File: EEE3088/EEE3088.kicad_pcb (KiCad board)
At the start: 2 copper layers, 6 parts, among them U1 LTR-303ALS-01, U2 LTR-303ALS-01

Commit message: Lecture_PCB_Updates
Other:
- board outline added: 177.8 x 83.8 mm
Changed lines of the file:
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@@
   )
   (setup
+    (stackup
+      (layer "F.SilkS" (type "Top Silk Screen"))
+      (layer "F.Paste" (type "Top Solder Paste"))
+      (layer "F.Mask" (type "Top Solder Mask") (thickness 0.01))
+      (layer "F.Cu" (type "copper") (thickness 0.035))
+      (layer "dielectric 1" (type "core") (thickness 1.51) (material "FR4") (epsilon_r 4.5) (loss_tangent 0.02))
+      (layer "B.Cu" (type "copper") (thickness 0.035))
+      (layer "B.Mask" (type "Bottom Solder Mask") (thickness 0.01))
+      (layer "B.Paste" (type "Bottom Solder Paste"))
+      (layer "B.SilkS" (type "Bottom Silk Screen"))
+      (copper_finish "None")
+      (dielectric_constraints no)
+    )
     (pad_to_mask_clearance 0)
     (pcbplotparams
@@
     )
   )
+  (gr_rect (start 40.64 43.18) (end 218.44 127)
+    (stroke (width 0.1) (type default)) (fill none) (layer "Edge.Cuts"))
 )

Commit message: Started Microcontroller PCB
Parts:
- added 0 Ohm: RESC1005X40N, 0 Ohm Resistor:RESC1005X40N, F.Cu at (148.4, 86.1)
- added 0 Ohm: RESC1005X40N, 0 Ohm Resistor:RESC1005X40N, F.Cu at (128.1, 98.8)
- added 1.8k Ohm: RESC2013X65N, 1.8k Ohm Resistor:RESC2013X65N, F.Cu at (125.6, 75.9)
- added 1.8k Ohm: RESC2013X65N, 1.8k Ohm Resistor:RESC2013X65N, F.Cu at (125.6, 81.0)
- added CH340G Bridge: SOIC127P600X180-16N, CH340G Bridge:SOIC127P600X180-16N, F.Cu at (140.8, 91.2)
- added EEPROM Chip: SOIC127P600X175-8N, AT24C256C-SSHL-T EEPROM Chip:SOIC127P600X175-8N, F.Cu at (125.4, 89.3)
- added MICROXNJ USB Interface: SHOUHAN_MICROXNJ, MICROXNJ USB Interface:SHOUHAN_MICROXNJ, F.Cu at (140.7, 74.1)
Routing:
- net (no net): track 0.00 -> 86.4 mm
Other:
- board text added: "5V from USB"
- board text added: "D-"
- board text added: "GND"
- board text added: "Microcontroller Interfacing Module"

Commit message: Finished uC PCB connections
Your mom helped
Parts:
- moved 1.8k Ohm 47.9 mm to (170.2, 63.5), turned to -90 degrees
- moved EEPROM Chip 42.7 mm to (154.9, 58.4)
- moved 0 Ohm 42.0 mm to (154.4, 66.0)
- moved 1.8k Ohm 39.9 mm to (162.6, 61.0), turned to -90 degrees
- moved CH340G Bridge 25.2 mm to (139.7, 66.0), turned to 90 degrees
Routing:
- net (no net): track 86.4 -> 309.4 mm
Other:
- board text added: "Needs to go to 3.3V"
- board text added: "Needs to go to GND"
- board text added: "RXD"
- board text added: "SCL"
- board text added: "SDA"
- board text added: "TIMIN"
- board text added: "TIMOUT"
- board text added: "TXD"
- board text removed: "Microcontroller Interfacing Module"

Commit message: pcb_Sense_Initial
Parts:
- added C3: 1uF, Capacitor_SMD:C_0805_2012Metric, F.Cu at (54.9, 95.2)
- added C4: 1uF, Capacitor_SMD:C_0805_2012Metric, F.Cu at (144.8, 95.2)
- added C9: 1uF, Capacitor_SMD:C_0805_2012Metric, F.Cu at (244.9, 109.6)
- added R10: 0, Resistor_SMD:R_0402_1005Metric, F.Cu at (226.0, 121.1)
- added R11: 0, Resistor_SMD:R_0402_1005Metric, F.Cu at (135.1, 137.2)
- added R12: 0, Resistor_SMD:R_0402_1005Metric, F.Cu at (66.5, 137.2)
- added R13: 0, Resistor_SMD:R_0402_1005Metric, F.Cu at (66.5, 55.9)
- added R18: 0, Resistor_SMD:R_0402_1005Metric, F.Cu at (60.5, 100.3)
- added R19: 0, Resistor_SMD:R_0402_1005Metric, F.Cu at (60.5, 99.1)
- added R20: 0, Resistor_SMD:R_0402_1005Metric, F.Cu at (140.5, 100.3)
- added R21: 0, Resistor_SMD:R_0402_1005Metric, F.Cu at (140.5, 99.1)
- added R22: 10K, Resistor_SMD:R_0805_2012Metric, F.Cu at (139.7, 106.7)
- added R23: 10K, Resistor_SMD:R_0805_2012Metric, F.Cu at (55.9, 107.6)
- added R24: 10K, Resistor_SMD:R_0805_2012Metric, F.Cu at (144.8, 106.7)
- added R25: 10K, Resistor_SMD:R_0805_2012Metric, F.Cu at (61.0, 107.6)
- added R26: 10K, Resistor_SMD:R_0805_2012Metric, F.Cu at (142.2, 106.7)
- added R27: 10K, Resistor_SMD:R_0805_2012Metric, F.Cu at (58.4, 107.6)
- added R30: 0, Resistor_SMD:R_0402_1005Metric, F.Cu at (259.2, 93.9)
- added R31: 0, Resistor_SMD:R_0402_1005Metric, F.Cu at (259.2, 95.9)
- added R4: 0, Resistor_SMD:R_0402_1005Metric, F.Cu at (226.0, 113.1)
- added R6: 0, Resistor_SMD:R_0402_1005Metric, F.Cu at (226.0, 115.1)
- added R8: 0, Resistor_SMD:R_0402_1005Metric, F.Cu at (226.0, 117.1)
- added R9: 0, Resistor_SMD:R_0402_1005Metric, F.Cu at (226.0, 119.1)
- added TP1: TestPoint, TestPoint:TestPoint_Pad_2.0x2.0mm, F.Cu at (245.2, 115.6)
- added TP10: TestPoint, TestPoint:TestPoint_Pad_2.0x2.0mm, F.Cu at (134.6, 97.8)
- added TP11: TestPoint, TestPoint:TestPoint_Pad_2.0x2.0mm, F.Cu at (64.8, 105.4)
- added TP13: TestPoint, TestPoint:TestPoint_Pad_2.0x2.0mm, F.Cu at (245.2, 95.4)
- added TP14: TestPoint, TestPoint:TestPoint_Pad_2.0x2.0mm, F.Cu at (245.2, 100.5)
- added TP15: TestPoint, TestPoint:TestPoint_Pad_2.0x2.0mm, F.Cu at (245.2, 105.5)
- added TP16: TestPoint, TestPoint:TestPoint_Pad_2.0x2.0mm, F.Cu at (250.2, 95.4)
- added TP17: TestPoint, TestPoint:TestPoint_Pad_2.0x2.0mm, F.Cu at (250.2, 100.5)
- added TP18: TestPoint, TestPoint:TestPoint_Pad_2.0x2.0mm, F.Cu at (250.2, 105.5)
- added TP19: TestPoint, TestPoint:TestPoint_Pad_2.0x2.0mm, F.Cu at (255.3, 95.4)
- added TP2: TestPoint, TestPoint:TestPoint_Pad_2.0x2.0mm, F.Cu at (245.2, 120.7)
- added TP20: TestPoint, TestPoint:TestPoint_Pad_2.0x2.0mm, F.Cu at (255.3, 100.5)
- added TP21: TestPoint, TestPoint:TestPoint_Pad_2.0x2.0mm, F.Cu at (255.3, 105.5)
- added TP22: TestPoint, TestPoint:TestPoint_Pad_2.0x2.0mm, F.Cu at (255.3, 120.7)
- added TP3: TestPoint, TestPoint:TestPoint_Pad_2.0x2.0mm, F.Cu at (250.2, 115.6)
- added TP4: TestPoint, TestPoint:TestPoint_Pad_2.0x2.0mm, F.Cu at (250.2, 120.7)
- added TP5: TestPoint, TestPoint:TestPoint_Pad_2.0x2.0mm, F.Cu at (255.3, 115.6)
- added TP6: TestPoint, TestPoint:TestPoint_Pad_2.0x2.0mm, F.Cu at (135.9, 66.0)
- added TP7: TestPoint, TestPoint:TestPoint_Pad_2.0x2.0mm, F.Cu at (64.8, 66.0)
- added TP8: TestPoint, TestPoint:TestPoint_Pad_2.0x2.0mm, F.Cu at (64.8, 97.8)
- added TP9: TestPoint, TestPoint:TestPoint_Pad_2.0x2.0mm, F.Cu at (134.6, 92.7)
- moved R17 226.2 mm to (142.2, 137.2), turned to -90 degrees
- moved U1 217.1 mm to (145.4, 100.7), turned to -90 degrees
- moved R16 206.8 mm to (142.2, 54.6), turned to -90 degrees
- moved R15 167.0 mm to (58.4, 137.2), turned to -90 degrees
- moved U2 138.1 mm to (55.2, 100.7), turned to -90 degrees
- moved R14 128.8 mm to (58.4, 54.6), turned to -90 degrees
- moved 0 Ohm 77.1 mm to (228.1, 43.2)
- moved CH340G Bridge 77.1 mm to (213.4, 43.2)
- moved 0 Ohm 77.1 mm to (222.1, 63.2)
- moved 1.8k Ohm 77.1 mm to (236.2, 38.1)
- moved 1.8k Ohm 77.1 mm to (243.8, 40.6)
- moved EEPROM Chip 77.1 mm to (228.6, 35.6)
- moved MICROXNJ USB Interface 77.1 mm to (214.4, 51.2)
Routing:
- net (no net): vias 0 -> 2
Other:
- board size 177.8 x 83.8 mm -> 100 x 100 mm

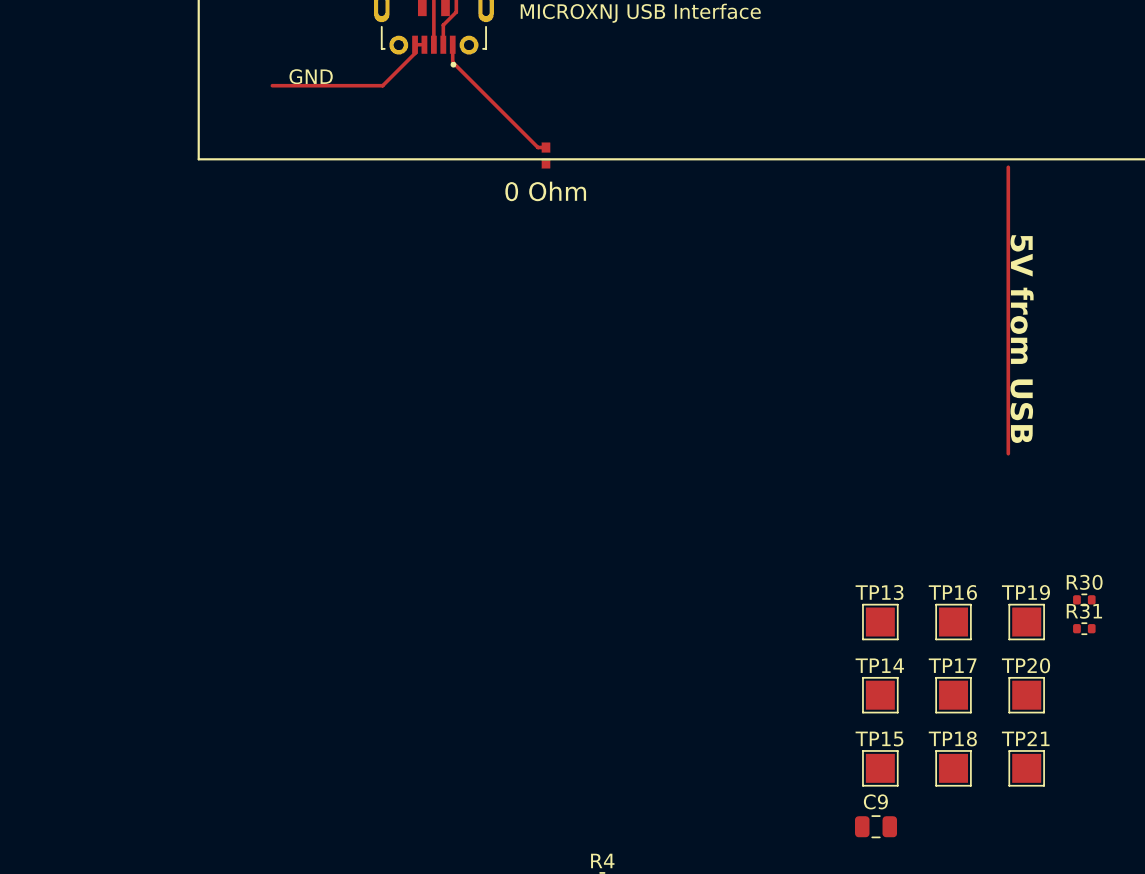
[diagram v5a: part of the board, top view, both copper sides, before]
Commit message: uC parts added onto PCB properly
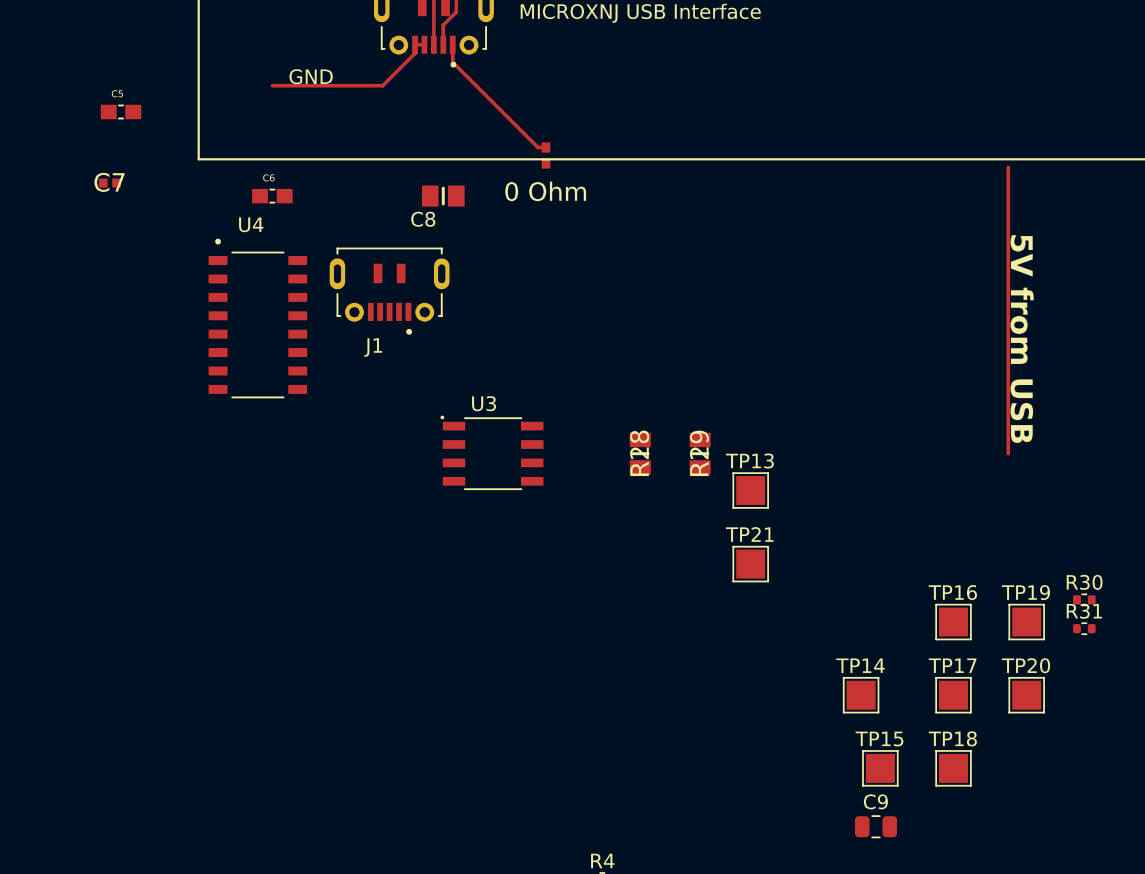
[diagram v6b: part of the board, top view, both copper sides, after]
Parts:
- added C5: 100nF, 100n CC0603KRX7R9BB104:CAPC1608X90, F.Cu at (192.8, 60.2)
- added C6: 100nF, 100n CC0603KRX7R9BB104:CAPC1608X90, F.Cu at (203.2, 66.0)
- added C7: 4.7uF, 4.7n Cap LIB_0402B472K500NT:CAPC1005X55N, F.Cu at (192.0, 65.1)
- added C8: 10nF, 10n Cap CL21B103KBANNNC:CAPC2012X140N, F.Cu at (215.0, 66.0)
- added J1: MICROXNJ, MICROXNJ:SHOUHAN_MICROXNJ, F.Cu at (211.3, 69.7)
- added R28: 1.8k, 1.8k Ohm Resistor:RESC2013X65N, F.Cu at (228.6, 83.8)
- added R29: 1.8k, 1.8k Ohm Resistor:RESC2013X65N, F.Cu at (232.7, 83.8)
- added U3: AT24C256C-SSHL-T, AT24C256C-SSHL-T EEPROM Chip:SOIC127P600X175-8N, F.Cu at (218.4, 83.8)
- added U4: CH340G, CH340G Bridge:SOIC127P600X180-16N, F.Cu at (202.2, 74.9)
- moved TP21 23.7 mm to (236.2, 91.4)
- moved TP13 12.7 mm to (236.2, 86.4)
- moved TP14 1.33 mm to (243.8, 100.5)

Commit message: Power PCB edit
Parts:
- added Battery-Charger1: TP4056, TP4056:SOP127P600X175-9N, F.Cu at (144.8, 132.1)
- added Battery-Holder1: BH-18650-PC, BH-18650-PC:BAT_BH-18650-PC, F.Cu at (99.1, 139.7)
- added C1: 10uF, CL10A106KP8NNNC:CAPC1608X90N, F.Cu at (139.7, 128.8)
- added C2: 10uF, CL10A106KP8NNNC:CAPC1608X90N, F.Cu at (139.7, 132.1)
- added LED1: Red, MyRedLED:LEDC1608X70N, F.Cu at (147.3, 144.8)
- added LED2: Green, MyGreenLED:LEDC1608X50N, F.Cu at (147.3, 139.7)
- added N-Mos1: AO3400A, MyNmos:SOT95P280X125-3N, F.Cu at (83.7, 125.8)
- added Op-Amp1: MCP6002T-I_SN, Myopamp:SOIC127P600X175-8N, F.Cu at (71.0, 124.5)
- added P-Mos1: AO3401A, MyPmos:SOT95P280X125-3N, F.Cu at (54.6, 143.2)
- added R2: 1.2k, My1.2k:RESC1608X55N, F.Cu at (147.3, 124.5)
- added R3: 100k, My100k:RESC3116X65N, F.Cu at (52.2, 147.3)
- added R32: 1k, My1.2k:RESC1608X55N, F.Cu at (142.2, 145.6)
- added R5: 1k, My1.2k:RESC1608X55N, F.Cu at (142.2, 140.5)
- added R7: 1M, My1M:RESC2013X65N, F.Cu at (88.9, 127.0)
- added V reg - 1: HT7533-1, HT7533-1:SOT89, F.Cu at (99.1, 126.1)
- added V reg - 2: HT7533-1, HT7533-1:SOT89, F.Cu at (109.2, 126.1)
- added Z1: MM3Z5V6C, MyZener:SODFL2513X100N, F.Cu at (58.4, 147.3)
- moved TP1 190.5 mm to (55.9, 137.2)
- moved TP22 176.8 mm to (78.6, 127.0)
- moved R4 174.3 mm to (53.3, 137.2), turned to 180 degrees
- moved TP3 159.2 mm to (91.4, 127.0)
- moved TP4 153.7 mm to (96.5, 119.4)
- moved TP5 146.1 mm to (109.2, 119.4)
- moved R8 134.8 mm to (91.3, 121.9)
- moved R10 130.1 mm to (96.0, 114.3)
- moved R9 117.4 mm to (108.7, 114.3), turned to 180 degrees
- moved TP2 106.8 mm to (139.7, 137.2)
- moved R6 90.4 mm to (139.7, 142.2), turned to 180 degrees
- moved TP15 34.7 mm to (213.4, 119.4)
- moved R11 29.0 mm to (142.8, 109.2)
- moved R15 25.5 mm to (55.9, 111.8)
- moved R17 25.5 mm to (144.8, 111.8)
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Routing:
- net +3.3V: track 0.00 -> 9.40 mm

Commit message: Power wires
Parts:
- moved R10 13.7 mm to (83.3, 119.4), turned to 180 degrees
- moved LED2 9.16 mm to (142.2, 147.3), turned to -90 degrees
- moved R32 9.16 mm to (147.3, 138.0)
- moved R2 3.59 mm to (144.8, 127.0)
- moved LED1 2.54 mm to (147.3, 147.3)
- turned R6 to -90 degrees
- turned Z1 to -90 degrees
- renumbered Battery-Charger1 to Bat-Charger
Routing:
- net /Power_Subsystem/V-pos: track 0.00 -> 50.8 mm
- net +5V: track 0.00 -> 46.5 mm
- net /Power_Subsystem/V-Reg: track 0.00 -> 19.7 mm
- net Net-(Voltage-Regulator-1-VO): track 0.00 -> 17.8 mm
- net Net-(Z1-K): track 0.00 -> 16.1 mm
- net Net-(Battery-Charger1-BAT): track 0.00 -> 13.8 mm
- net Net-(N-Mos1-Pad2): track 0.00 -> 13.0 mm
- net /Power_Subsystem/3.3-back: track 0.00 -> 11.5 mm
- net Net-(Z1-A): track 0.00 -> 11.2 mm
- net Net-(Voltage-Regulator-2-VO): track 0.00 -> 10.4 mm
- net Net-(Op-Amp1-VOUTA): track 0.00 -> 9.31 mm
- net Net-(Battery-Holder1-PadP): track 0.00 -> 8.22 mm
- net Net-(LED1-Pad1): track 0.00 -> 7.81 mm
- net Net-(Battery-Charger1-~{STDBY}): track 0.00 -> 5.93 mm
- net /Power_Subsystem/Vbat: track 0.00 -> 5.45 mm
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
